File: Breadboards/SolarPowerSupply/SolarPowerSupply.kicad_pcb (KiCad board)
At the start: 2 copper layers, 49 parts, among them P101 CONN_01X03, P102 CONN_01X07, U101 bq25504, U102 TPS63051, U103 TPS63050

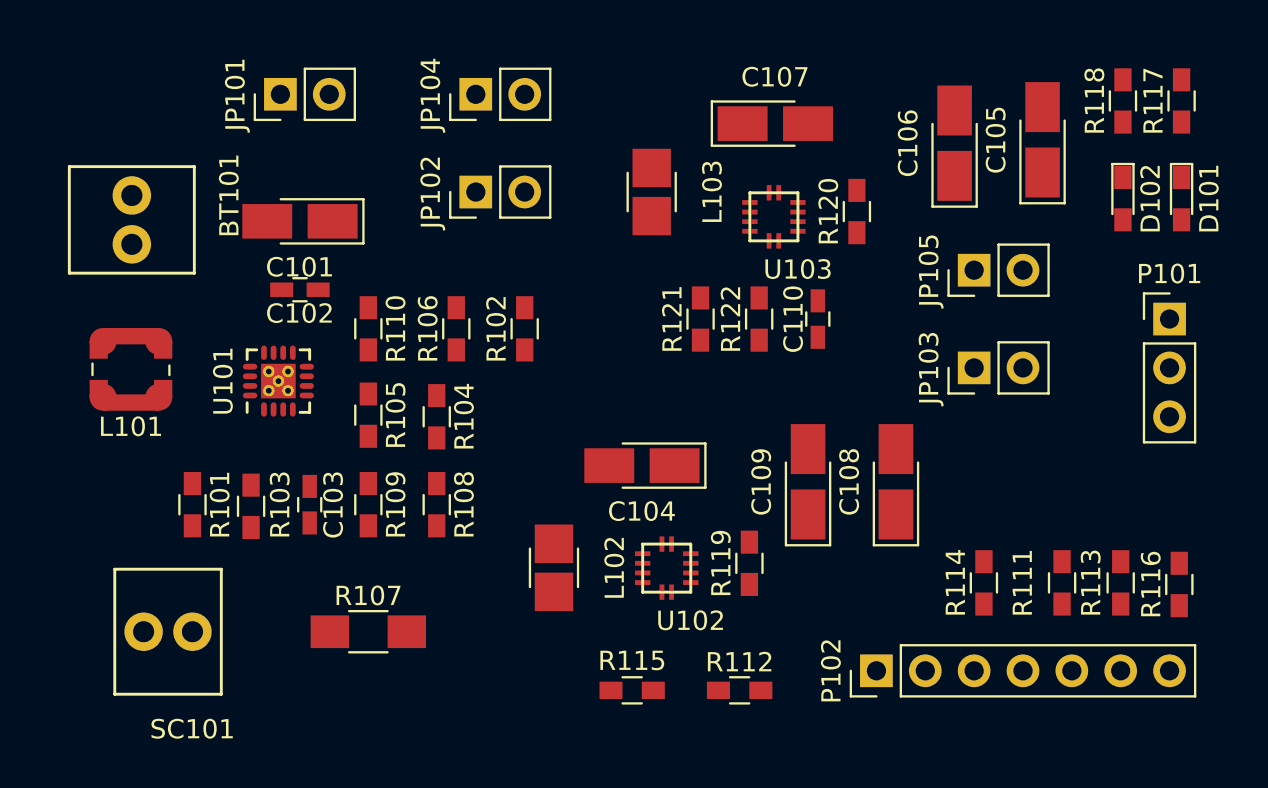
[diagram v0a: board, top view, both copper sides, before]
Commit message: First version of Power supply BB Layout
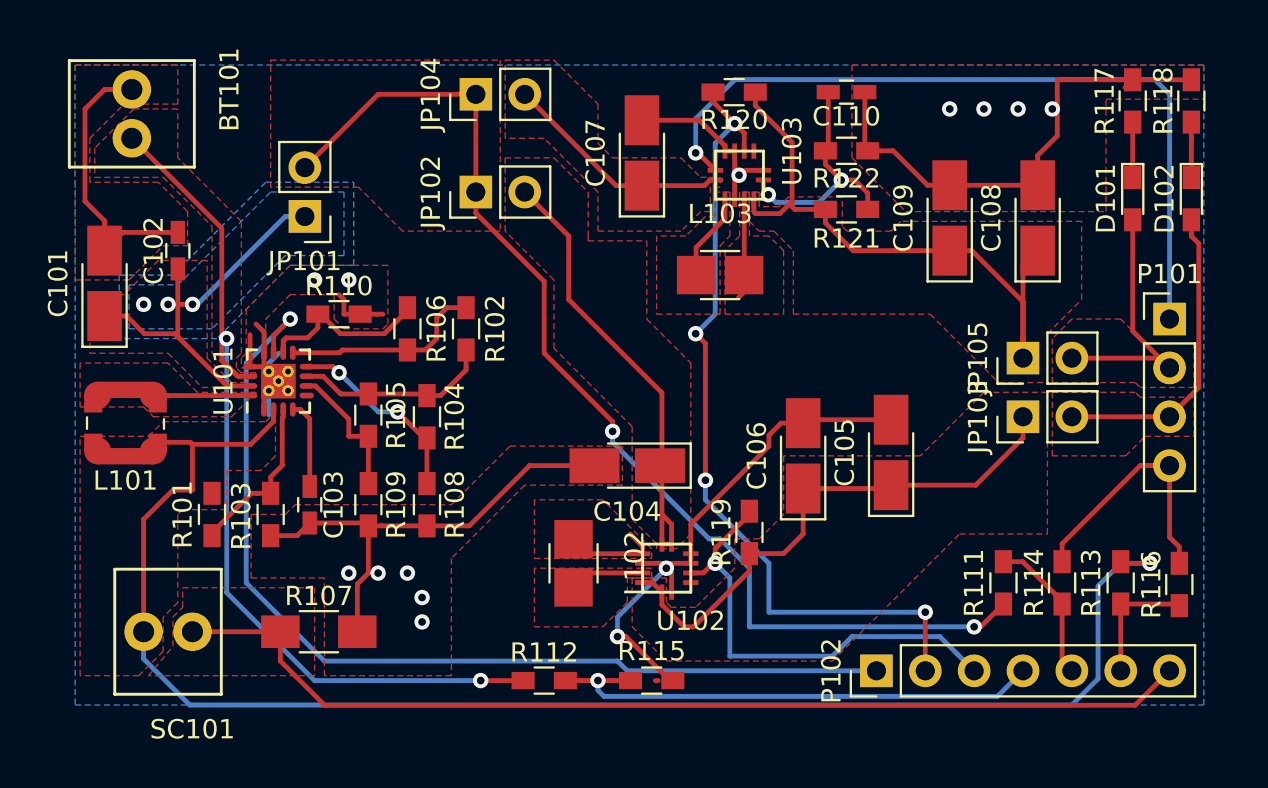
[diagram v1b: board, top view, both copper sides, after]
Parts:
- P101: value CONN_01X03 -> CONN_01X04; footprint Pin_Headers:Pin_Header_Straight_1x03_Pitch2.54mm -> Pin_Headers:Pin_Header_Straight_1x04_Pitch2.54mm
- moved C105 18.1 mm to (83.6, 119.2)
- moved C106 18.1 mm to (79.0, 119.4)
- moved C108 15.6 mm to (91.2, 107.0)
- moved C109 15.6 mm to (86.6, 107.0)
- moved C110 11.9 mm to (81.2, 100.5), turned to 0 degrees
- moved C101 10.7 mm to (42.7, 110.4), turned to 90 degrees
- moved R112 10.2 mm to (65.5, 131.1)
- moved R122 9.86 mm to (81.2, 103.5), turned to 180 degrees
- moved R121 9.49 mm to (81.2, 106.6), turned to 0 degrees
- moved R120 8.90 mm to (75.4, 100.5), turned to 180 degrees
- moved C107 7.10 mm to (70.6, 103.6), turned to 90 degrees
- moved C102 6.67 mm to (46.5, 108.7), turned to 90 degrees
- moved JP101 6.48 mm to (53.1, 106.9), turned to 180 degrees
- moved L103 5.59 mm to (74.7, 110.0), turned to 0 degrees
- moved BT101 5.51 mm to (44.1, 102.9)
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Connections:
- P101 pad 1: +5V -> 5V_Enable
- P101 pad 2: +3V3 -> +5V
- P101 pad 3: GND -> +3V3
- U101 pad 17: (no net) -> GND
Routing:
- net GND: track 0.00 -> 134.1 mm, vias 0 -> 14
- net /VSolar: track 0.00 -> 80.7 mm, vias 0 -> 1
- net /VBus: track 0.00 -> 58.1 mm, vias 0 -> 2
- net HK_SOLAR_I: track 0.00 -> 54.0 mm
- net BAT_OK: track 0.00 -> 51.4 mm, vias 0 -> 1
- net /VBat: track 0.00 -> 45.8 mm, vias 0 -> 2
- net PGOOD_5: track 0.00 -> 42.7 mm, vias 0 -> 4
- net 5V_Enable: track 0.00 -> 41.5 mm, vias 0 -> 1
- net Net-(C108-Pad1): track 0.00 -> 34.1 mm
- net Net-(C105-Pad1): track 0.00 -> 28.4 mm
- net HK_BAT_V: track 0.00 -> 26.7 mm, vias 0 -> 1
- net PGOOD_3.3: track 0.00 -> 23.9 mm, vias 0 -> 1
- net Net-(C104-Pad1): track 0.00 -> 23.5 mm
- net Net-(C101-Pad1): track 0.00 -> 21.1 mm, vias 0 -> 3
- net +3V3: track 0.00 -> 16.1 mm
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- added copper zone on F.Cu, net +3V3
- added copper zone on F.Cu, net +5V
- added copper zone on F.Cu, net /VBat
- added copper zone on F.Cu, net /VBus
- added copper zone on F.Cu, net /VSolar
- added copper zone on B.Cu, net GND
- added copper zone on F.Cu, net GND
- added copper zone on F.Cu, net HK_SOLAR_I
- added copper zone on B.Cu, net Net-(C101-Pad1)
- added copper zone on F.Cu, net Net-(C101-Pad1)
- added copper zone on F.Cu, net Net-(C104-Pad1)
- added copper zone on F.Cu, net Net-(C105-Pad1)
- added copper zone on F.Cu, net Net-(C107-Pad1)
- added copper zone on F.Cu, net Net-(C108-Pad1)
- added copper zone on F.Cu, net Net-(L101-Pad2)
- added copper zone on F.Cu, net Net-(L102-Pad1)
- added copper zone on F.Cu, net Net-(L102-Pad2)
- added copper zone on F.Cu, net Net-(L103-Pad1)
- added copper zone on F.Cu, net Net-(L103-Pad2)

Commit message: Modified layout around bq25504
In order to be more in accordance with the layout guidelines as listed in the
bq25504 datasheet, the layout around the mentioned chip was reworked.
Mainly the CStor and CBypass as well as the inductor were replaced.
The pouring of ground and supply planes was also redone.
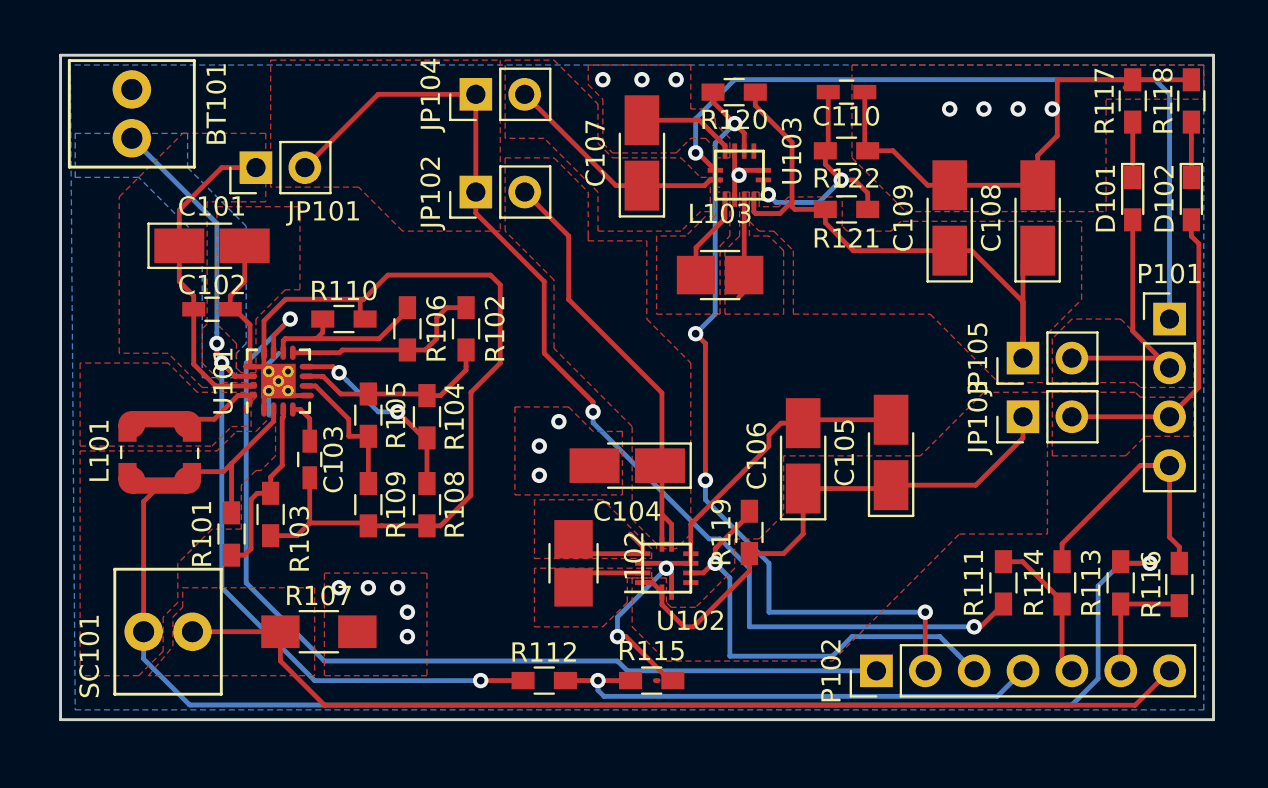
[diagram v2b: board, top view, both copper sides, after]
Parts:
- moved C101 5.92 mm to (48.3, 108.5), turned to 0 degrees
- moved JP101 3.59 mm to (50.5, 104.4), turned to 90 degrees
- moved C102 3.53 mm to (48.3, 111.8), turned to 0 degrees
- moved C103 2.35 mm to (53.3, 119.6)
- moved L101 2.34 mm to (45.5, 119.2)
- moved R101 1.44 mm to (49.3, 123.4)
- moved R110 0.36 mm to (55.1, 112.3)
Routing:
- net Net-(C101-Pad1): track 21.1 -> 16.6 mm, vias 3 -> 0
- net GND: track 134.1 -> 138.0 mm, vias 14 -> 18
- net Net-(C103-Pad1): track 4.60 -> 2.25 mm
- net Net-(L101-Pad2): track 4.98 -> 6.14 mm
- net /VSolar: track 80.7 -> 79.6 mm
- net /VBat: track 45.8 -> 44.7 mm, vias 2 -> 3
- net Net-(R101-Pad2): track 8.68 -> 9.49 mm
- added copper zone on B.Cu, net /VBat
- removed copper zone on F.Cu, net /VBat
- removed copper zone on B.Cu, net Net-(C101-Pad1)
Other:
- board outline added: 59.9 x 34.5 mm
